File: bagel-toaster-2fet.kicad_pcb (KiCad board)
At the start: 2 copper layers, 138.4 x 93.3 mm, 120 parts, among them J1 9v, J10 i2, J11 o1s, J12 o1, J13 i1, J14 i2s, J15 i1s, J16 o2s, J17 o2, J18 gnd, J19 bs, J2 gnd, J20 9v, J21 gnd, J22 9v, J23 gnd, J24 bs, J25 in, J26 out, J27 do_rtn, J28 do_snd, J29 gnd, J3 i1b, J30 gnd, J31 gnd, J32 9v, J4 o1b, J5 9v, J6 9v, J7 i2b, J8 o2b, J9 9v, Q1 J201, Q2 J113, SW1 Alpha_3PDT, SW2 Alpha_3PDT, SW3 Alpha_3PDT, SW4 3pdt, U1 4069, U2 TL074

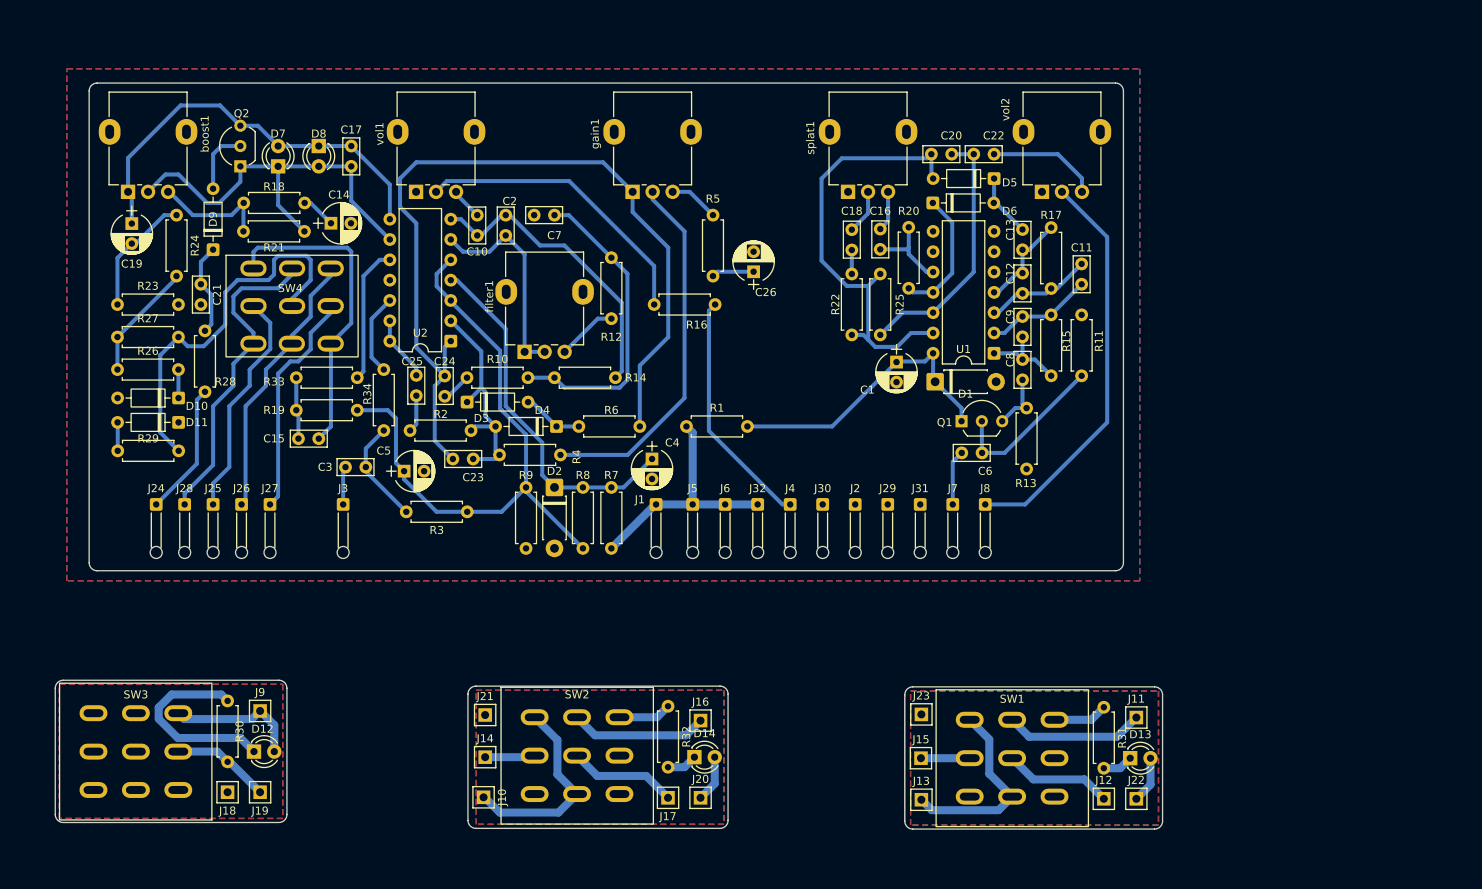
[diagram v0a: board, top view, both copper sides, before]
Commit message: add sag control and reannotate
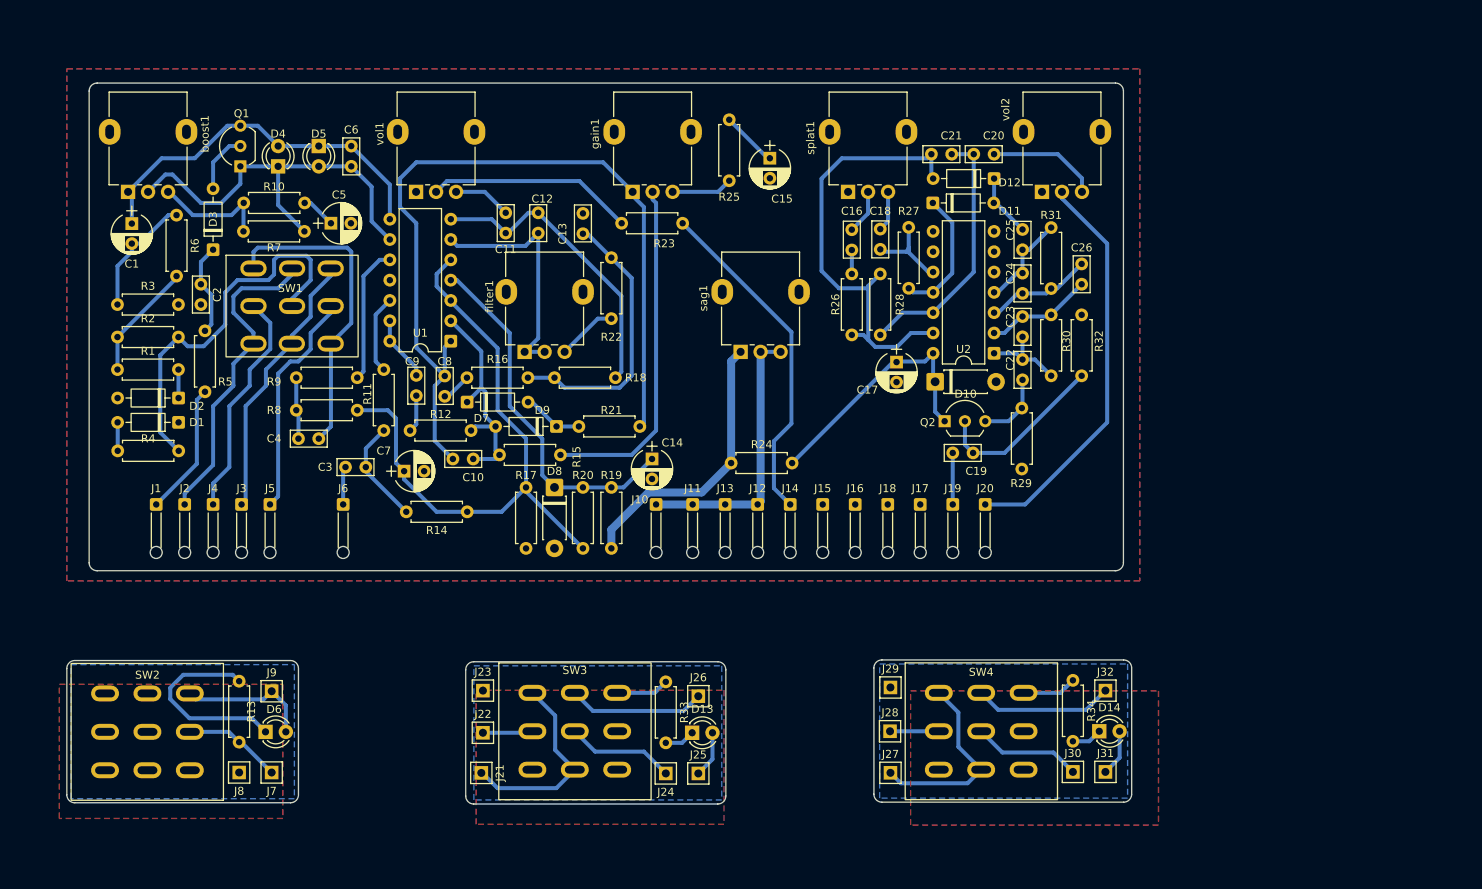
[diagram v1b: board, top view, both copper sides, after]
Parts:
- added sag1: 10k, Potentiometer_THT:Potentiometer_Alpha_RD901F-40-00D_Single_Vertical, F.Cu at (151.8, 67.4)
- C10: renamed from C23; value 1n -> 100p
- moved C15 14.3 mm to (155.4, 43.2), turned to -90 degrees
- moved R23 10.9 mm to (144.5, 51.3)
- moved R24 7.22 mm to (150.6, 81.3)
- moved C13 6.10 mm to (132.1, 50.1), turned to -90 degrees
- moved J32 5.12 mm to (197.4, 109.7)
- moved R34 5.12 mm to (193.3, 108.4)
- moved D14 5.12 mm to (196.6, 114.8)
- moved J28 5.12 mm to (170.5, 114.8)
- moved J30 5.12 mm to (193.3, 119.9)
- moved J31 5.12 mm to (197.4, 119.9)
- moved SW4 5.12 mm to (181.9, 114.8)
- moved J29 5.12 mm to (170.5, 109.3)
- moved J27 5.12 mm to (170.5, 120.0)
- moved R25 4.76 mm to (150.4, 46.0), turned to 90 degrees
- moved C12 4.07 mm to (126.5, 52.5)
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- renumbered C19 to C1, C10 to C11, C2 to C12, C7 to C13, C4 to C14, C26 to C15, C18 to C16, C1 to C17, C16 to C18, C6 to C19, C21 to C2, C22 to C20, C20 to C21, C8 to C22, C9 to C23, C12 to C24, C13 to C25, C11 to C26, C15 to C4, C14 to C5, C17 to C6, C5 to C7, C24 to C8, C25 to C9, D11 to D1, D1 to D10, D6 to D11, D5 to D12, D14 to D13, D13 to D14, D10 to D2, D9 to D3, D7 to D4, D8 to D5, D12 to D6, D3 to D7, D2 to D8, D4 to D9, J24 to J1, J1 to J10, J5 to J11, J32 to J12, J6 to J13, J4 to J14, J30 to J15, J2 to J16, J31 to J17, J29 to J18, J7 to J19, J28 to J2, J8 to J20, J10 to J21, J14 to J22, J21 to J23, J17 to J24, J20 to J25, J16 to J26, J13 to J27, J15 to J28, J23 to J29, J26 to J3, J12 to J30, J22 to J31, J11 to J32, J25 to J4, J27 to J5, J3 to J6, J19 to J7, J18 to J8, Q2 to Q1, Q1 to Q2, R26 to R1, R18 to R10, R34 to R11, R2 to R12, R30 to R13, R3 to R14, R4 to R15, R10 to R16, R9 to R17, R14 to R18, R7 to R19, R27 to R2, R8 to R20, R6 to R21, R12 to R22, R16 to R23, R1 to R24, R5 to R25, R22 to R26, R20 to R27, R25 to R28, R13 to R29, R23 to R3, R15 to R30, R17 to R31, R11 to R32, R32 to R33, R31 to R34, R29 to R4, R28 to R5, R24 to R6, R21 to R7, R19 to R8, R33 to R9, SW4 to SW1, SW3 to SW2, SW2 to SW3, SW1 to SW4, U2 to U1, U1 to U2
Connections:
- R19 pad 1: /9v -> Net-(R1-Pad1)
- R24 pad 1: /9v -> Net-(R1-Pad1)
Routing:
- net Net-(R1-Pad1): track 0.00 -> 35.2 mm
- net Net-(J4-Pin_1): track 30.1 -> 42.5 mm
- net Net-(R16-Pad2): track 37.0 -> 25.9 mm
- net Net-(D7-A): track 52.3 -> 47.7 mm
- net /v1: track 37.0 -> 32.4 mm
- net Net-(C7-Pad2): track 38.8 -> 34.7 mm
- net /9v: track 30.6 -> 34.4 mm
- net Net-(U2B--): track 26.4 -> 30.0 mm
- net Net-(C10-Pad2): track 4.01 -> 7.29 mm
- net Net-(R4-Pad2): track 45.9 -> 43.2 mm
- net /gainOut: track 107.6 -> 105.1 mm
- net Net-(C26-Pad1): track 5.31 -> 7.07 mm
- net Net-(Q1-G): track 20.4 -> 21.9 mm
- net Net-(R5-Pad1): track 6.25 -> 7.65 mm
- net Net-(Q1-S): track 7.47 -> 8.81 mm
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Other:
- board size 138.4 x 93.3 mm -> 133.1 x 90.1 mm

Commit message: 16mm pot refactor done
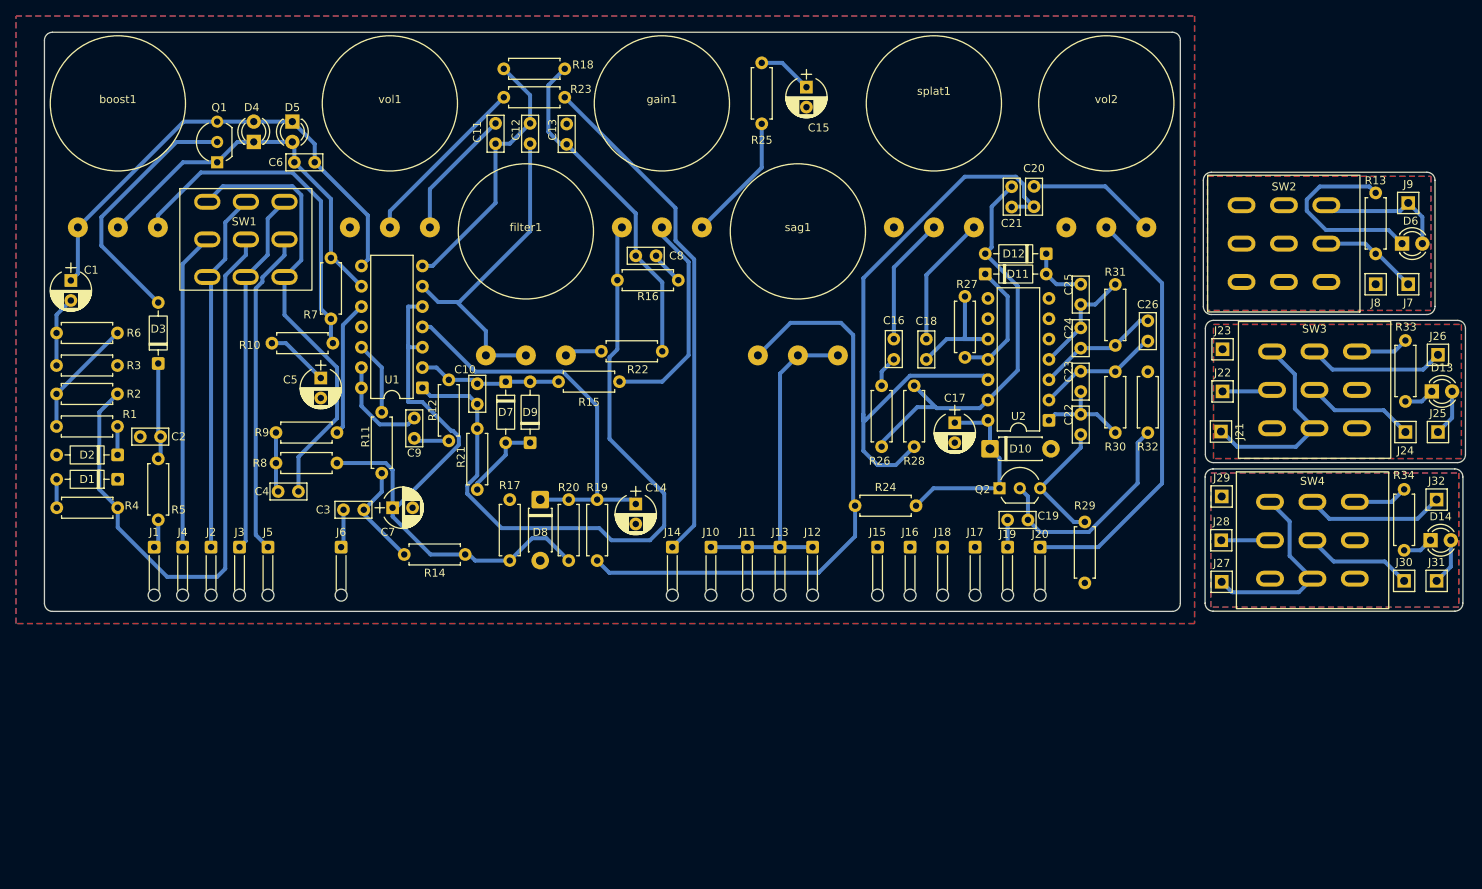
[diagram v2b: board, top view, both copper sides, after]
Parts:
- boost1, filter1, gain1, sag1, splat1, vol1, vol2: footprint Potentiometer_THT:Potentiometer_Alpha_RD901F-40-00D_Single_Vertical -> 1_mylib-footprint:pot-16mm-short-leg
- moved D6 154.6 mm to (234.5, 53.8)
- moved J7 154.6 mm to (235.2, 58.9)
- moved J8 154.6 mm to (231.2, 58.9)
- moved J9 154.6 mm to (235.2, 48.8)
- moved R13 154.6 mm to (231.2, 55.1)
- moved SW2 154.6 mm to (219.7, 53.8)
- moved J21 101.8 mm to (211.8, 77.3)
- moved J22 101.8 mm to (212.0, 72.3)
- moved J23 101.8 mm to (212.0, 67.1)
- moved SW3 101.8 mm to (223.5, 72.1)
- moved D13 101.8 mm to (238.2, 72.3)
- moved J24 101.8 mm to (234.9, 77.4)
- moved J25 101.8 mm to (239.0, 77.4)
- moved J26 101.8 mm to (239.0, 67.8)
- moved R33 101.8 mm to (234.9, 66.0)
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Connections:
- C13 pad 2: Net-(C7-Pad2) -> Net-(C13-Pad2)
- C8 pad 1: /gainOut -> Net-(C13-Pad2)
- C8 pad 2: Net-(C24-Pad2) (its old number) -> Net-(C8-Pad2)
- R16 pad 1: Net-(C24-Pad2) (its old number) -> /gainOut
- R16 pad 2: Net-(C7-Pad2) -> Net-(C8-Pad2)
- R18 pad 1: Net-(C7-Pad2) -> Net-(C13-Pad2)
- R22 pad 1: Net-(C7-Pad2) -> Net-(C13-Pad2)
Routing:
- net Net-(C20-Pad1): track 32.4 -> 80.3 mm
- net Net-(C13-Pad2): track 0.00 -> 42.5 mm
- net Net-(R19-Pad1): track 35.2 -> 74.3 mm
- net Net-(C7-Pad2): track 34.7 -> 0.00 mm
- net Net-(R10-Pad2): track 14.9 -> 44.0 mm
- net /b_rtn: track 48.2 -> 77.2 mm
- net Net-(D3-A): track 7.55 -> 32.0 mm
- net Net-(J14-Pin_1): track 42.5 -> 64.1 mm
- net /gainOut: track 105.1 -> 88.0 mm
- net /b_snd: track 39.8 -> 55.7 mm
- net Net-(R15-Pad2): track 43.2 -> 27.4 mm
- net Net-(D4-A): track 47.7 -> 61.6 mm
- net Net-(J1-Pin_1): track 16.6 -> 3.62 mm
- net Net-(U1B--): track 30.0 -> 42.1 mm
- net /d_rtn: track 28.5 -> 40.6 mm
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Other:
- board size 133.1 x 90.1 mm -> 177.6 x 72.4 mm

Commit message: .
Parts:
- C15: value 100u -> 1u
- moved D6 161.5 mm to (87.2, 120.1)
- moved J7 161.5 mm to (87.9, 125.2)
- moved J8 161.5 mm to (83.9, 125.2)
- moved J9 161.5 mm to (87.9, 115.1)
- moved R13 161.5 mm to (83.9, 121.4)
- moved SW2 161.5 mm to (72.4, 120.1)
- moved D13 107.1 mm to (143.5, 122.4)
- moved J21 107.1 mm to (117.1, 127.4)
- moved J22 107.1 mm to (117.3, 122.4)
- moved J23 107.1 mm to (117.3, 117.1)
- moved J24 107.1 mm to (140.2, 127.4)
- moved R33 107.1 mm to (140.2, 116.0)
- moved SW3 107.1 mm to (128.8, 122.2)
- moved J25 107.1 mm to (144.2, 127.4)
- moved J26 106.9 mm to (144.3, 117.3)
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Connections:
- R12 pad 1: Net-(C9-Pad1) -> Net-(D7-K)
- R12 pad 2: Net-(D7-K) -> Net-(C9-Pad1)
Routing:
- net Net-(R19-Pad1): track 74.3 -> 12.7 mm
- net Net-(R10-Pad2): track 44.0 -> 14.0 mm
- net Net-(R15-Pad2): track 27.4 -> 55.3 mm
- net Net-(J6-Pin_1): track 4.79 -> 32.5 mm
- net Net-(D4-K): track 48.1 -> 67.4 mm
- net Net-(D4-A): track 61.6 -> 80.3 mm
- net /gainOut: track 88.0 -> 69.7 mm
- net Net-(J14-Pin_1): track 64.1 -> 81.9 mm
- net /v1: track 24.7 -> 39.6 mm
- net /v2: track 49.8 -> 38.3 mm
- net Net-(R25-Pad1): track 16.0 -> 4.85 mm
- net Net-(J20-Pin_1): track 53.4 -> 61.8 mm
- net Net-(D3-A): track 32.0 -> 39.7 mm
- net Net-(C20-Pad1): track 80.3 -> 73.2 mm
- net Net-(U1D--): track 12.7 -> 5.59 mm
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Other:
- board size 177.6 x 72.4 mm -> 144.4 x 105.1 mm
